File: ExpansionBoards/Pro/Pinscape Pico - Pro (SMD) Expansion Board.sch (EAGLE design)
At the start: 209 parts, among them IC1 UCC27523D, IC10 UCC27523D, IC11 UCC27523D, IC12 UCC27523D, IC13 UCC27523D, IC14 UCC27523D, IC15 TLC59116FIRHBR, IC16 TLC59116FIRHBR, IC17 TLC59116FIRHBR, IC18 TLC59116FIRHBR, IC19 ULN2803ADWR, IC2 UCC27523D, IC20 ULN2803ADWR, IC21 ULN2803ADWR, IC22 ULN2803ADWR, IC23 ULN2803ADWR, IC24 SN74HC165PWR, IC25 SN74HC165PWR, IC26 SN74HC165PWR, IC27 SN74HC165PWR, IC28 LIS3DHTR, IC29 SN74LVC1G175DCKR, IC3 UCC27523D, IC30 APX809S-29SA-7, IC31 LTV-827S, IC32 ADS1115IDGSR, IC33 TLV75733PDBVR, IC34 RV-3032-C7, IC4 UCC27523D, IC5 UCC27523D, IC6 UCC27523D, IC7 UCC27523D, IC8 UCC27523D, IC9 UCC27523D, J1 640445-6, J10 1-640456-0, J11 1-640456-0, J12 1-640456-0, J13 640445-5, J14 640445-9, J15 640445-9, J16 640445-9, J2 30316-6002HB, J3 1-640456-0, J4 640456-9, J5 640456-9, J6 640454-2, J7 215079-4, J8 30308-6002HB, J9 1-640456-0, Q1 BUK7K89-100EX, Q10 BUK7K89-100EX, Q11 BUK7K89-100EX, Q12 BUK7K89-100EX, Q13 BUK7K89-100EX, Q14 BUK7K89-100EX, Q15 UMA5NTR, Q16 UMA5NTR, Q17 UMA5NTR, Q18 UMA5NTR, Q19 UMA5NTR, Q2 BUK7K89-100EX, Q20 UMA5NTR, Q21 UMA5NTR, Q22 UMA5NTR, Q23 UMA5NTR, Q24 UMA5NTR, Q25 UMA5NTR, Q26 UMA5NTR, Q27 DSS8110Y-7, Q3 BUK7K89-100EX, Q4 BUK7K89-100EX, Q5 BUK7K89-100EX, Q6 BUK7K89-100EX, Q7 BUK7K89-100EX, Q8 BUK7K89-100EX, Q9 BUK7K89-100EX, SW1 TS-1187A-B-A-B, U1 BAT-HLD-001-THM

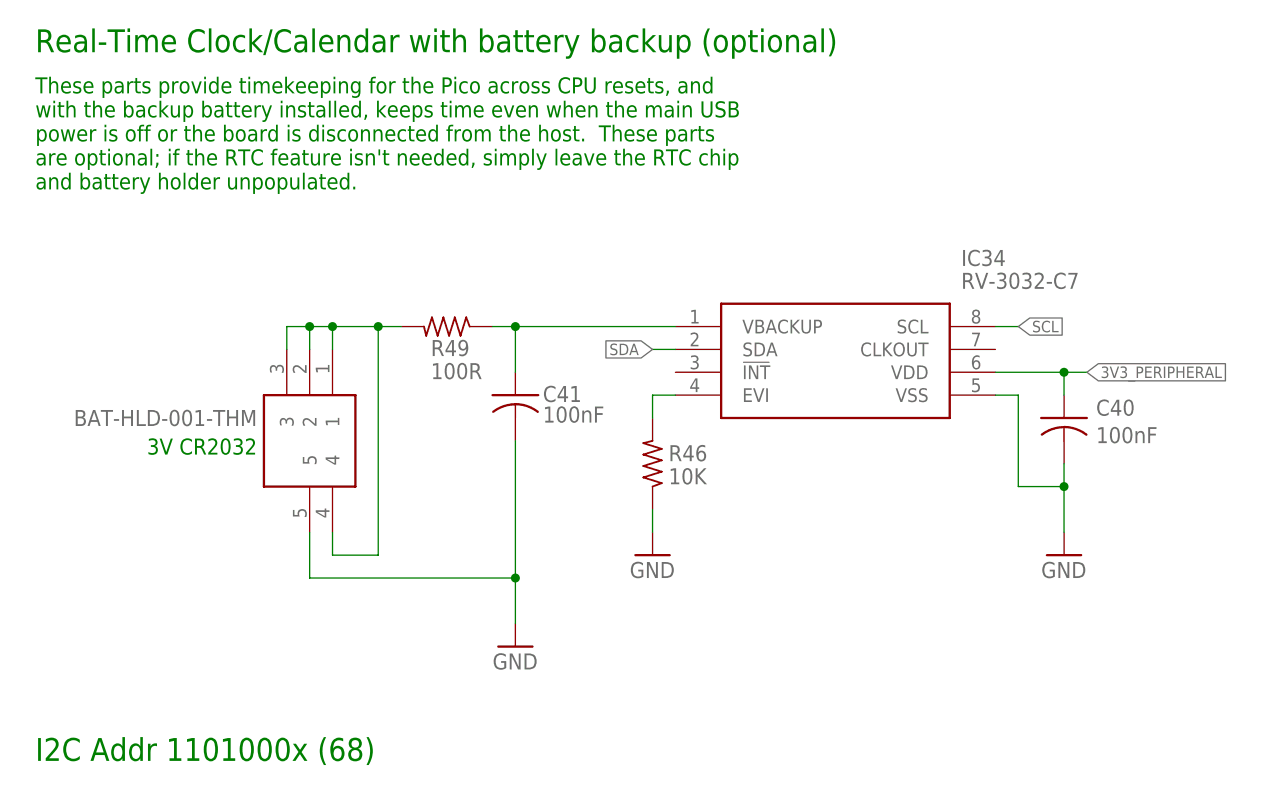
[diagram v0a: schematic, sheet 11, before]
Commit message: exp board: pro: change battery holder to top clip type
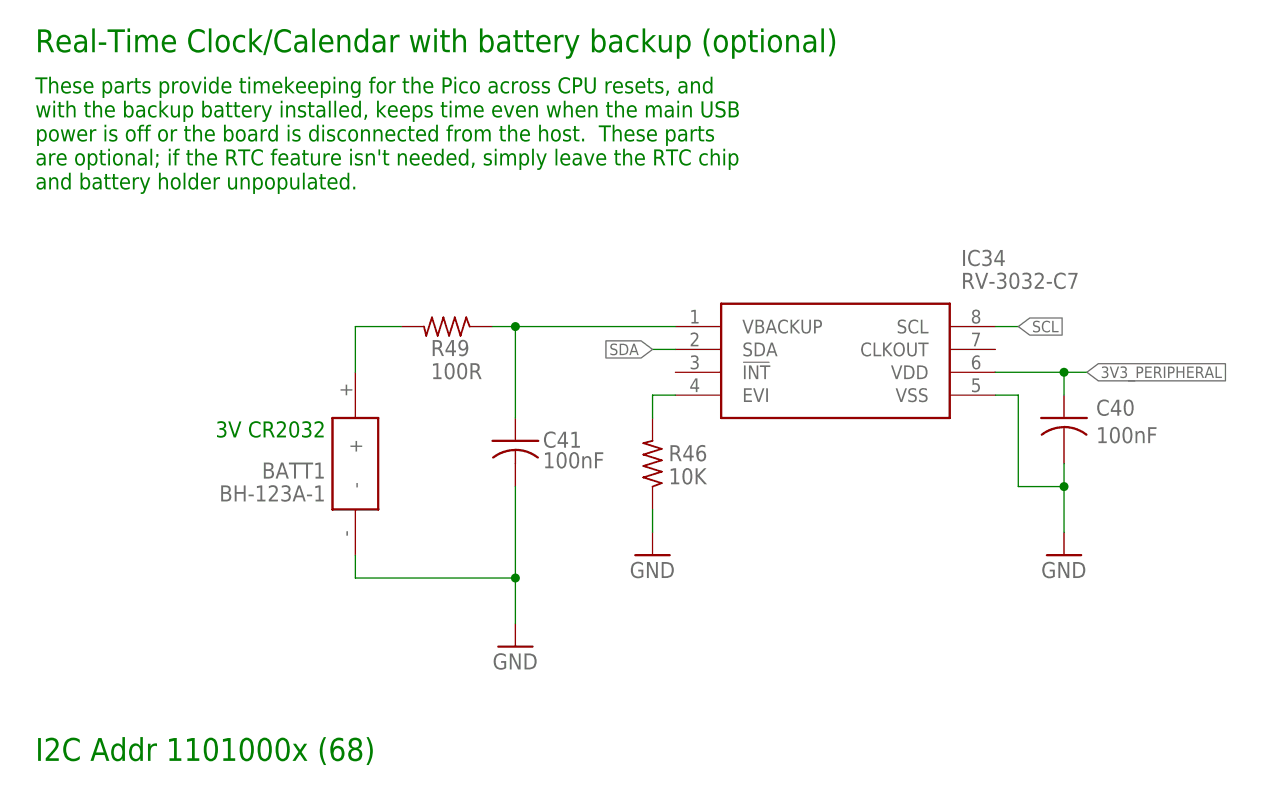
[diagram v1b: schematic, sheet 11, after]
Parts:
- removed U1: BAT-HLD-001-THM, SamacSys_Parts:BAT-HLD-001-THM
- added BATT1: BH-123A-1, SamacSys_Parts:BH-123A-1
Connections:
- net GND: now also BATT1.-; no longer U1.5
- net N$72: now also BATT1.+; no longer U1.1, U1.2, U1.3, U1.4
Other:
- moved on the sheet: C41
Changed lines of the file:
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@@
 <part name="R45" library="resistor" deviceset="R-US_" device="R0603" value="10K"/>
 <part name="C40" library="rcl" deviceset="C-US" device="C0402" value="100nF"/>
-<part name="U1" library="SamacSys_Parts" deviceset="BAT-HLD-001-THM" device=""/>
 <part name="GND30" library="supply1" deviceset="GND" device=""/>
 <part name="GND53" library="supply1" deviceset="GND" device=""/>
@@
 <part name="GND11" library="supply1" deviceset="GND" device=""/>
 <part name="GND12" library="supply1" deviceset="GND" device=""/>
+<part name="BATT1" library="SamacSys_Parts" deviceset="BH-123A-1" device=""/>
 </parts>
 <sheets>
@@
 <description>RTC (Real-time clock)</description>
 <plain>
-<text x="29.718" y="53.594" size="1.778" layer="91" rot="R180">3V CR2032</text>
+<text x="37.338" y="54.61" size="1.778" layer="91" align="center-right">3V CR2032</text>
 <text x="5.08" y="17.78" size="2.54" layer="91">I2C Addr 1101000x (68)</text>
 <text x="5.08" y="96.52" size="2.54" layer="91">Real-Time Clock/Calendar with battery backup (optional)</text>
@@
 <attribute name="VALUE" x="122.936" y="53.086" size="1.778" layer="96"/>
 </instance>
-<instance part="U1" gate="G$1" x="38.1" y="63.5" smashed="yes" rot="R270">
-<attribute name="VALUE" x="29.718" y="55.88" size="1.778" layer="96" rot="R180" align="center-left"/>
-</instance>
 <instance part="GND30" gate="1" x="58.42" y="30.48"/>
 <instance part="GND53" gate="1" x="119.38" y="40.64"/>
-<instance part="C41" gate="G$1" x="58.42" y="58.42" smashed="yes">
-<attribute name="NAME" x="61.468" y="57.658" size="1.778" layer="95"/>
-<attribute name="VALUE" x="61.468" y="55.372" size="1.778" layer="96"/>
+<instance part="C41" gate="G$1" x="58.42" y="53.34" smashed="yes">
+<attribute name="NAME" x="61.468" y="52.578" size="1.778" layer="95"/>
+<attribute name="VALUE" x="61.468" y="50.292" size="1.778" layer="96"/>
 </instance>
 <instance part="IC34" gate="G$1" x="76.2" y="66.04"/>
@@
 <attribute name="VALUE" x="49.022" y="61.976" size="1.778" layer="96" rot="MR180"/>
 </instance>
+<instance part="BATT1" gate="G$1" x="40.64" y="50.8" smashed="yes" rot="R270">
+<attribute name="NAME" x="37.338" y="50.038" size="1.778" layer="95" rot="R180" align="center-left"/>
+<attribute name="VALUE" x="37.338" y="47.498" size="1.778" layer="96" rot="R180" align="center-left"/>
+</instance>
 </instances>
 <busses>
@@
 <net name="GND" class="0">
 <segment>
-<pinref part="U1" gate="G$1" pin="5"/>
 <pinref part="GND30" gate="1" pin="GND"/>
-<wire x1="35.56" y1="43.18" x2="35.56" y2="38.1" width="0.1524" layer="91"/>
 <pinref part="C41" gate="G$1" pin="2"/>
-<wire x1="58.42" y1="53.34" x2="58.42" y2="38.1" width="0.1524" layer="91"/>
-<wire x1="58.42" y1="38.1" x2="35.56" y2="38.1" width="0.1524" layer="91"/>
+<wire x1="58.42" y1="48.26" x2="58.42" y2="38.1" width="0.1524" layer="91"/>
+<pinref part="BATT1" gate="G$1" pin="-"/>
+<wire x1="58.42" y1="38.1" x2="58.42" y2="33.02" width="0.1524" layer="91"/>
+<wire x1="40.64" y1="40.64" x2="40.64" y2="38.1" width="0.1524" layer="91"/>
+<wire x1="40.64" y1="38.1" x2="58.42" y2="38.1" width="0.1524" layer="91"/>
 <junction x="58.42" y="38.1"/>
-<wire x1="58.42" y1="33.02" x2="58.42" y2="38.1" width="0.1524" layer="91"/>
 </segment>
 <segment>
@@
 </segment>
 </net>
-<net name="N$72" class="0">
-<segment>
-<pinref part="U1" gate="G$1" pin="4"/>
-<wire x1="38.1" y1="43.18" x2="38.1" y2="40.64" width="0.1524" layer="91"/>
-<wire x1="38.1" y1="40.64" x2="43.18" y2="40.64" width="0.1524" layer="91"/>
-<wire x1="43.18" y1="40.64" x2="43.18" y2="66.04" width="0.1524" layer="91"/>
-<pinref part="U1" gate="G$1" pin="1"/>
-<wire x1="38.1" y1="63.5" x2="38.1" y2="66.04" width="0.1524" layer="91"/>
-<pinref part="U1" gate="G$1" pin="2"/>
-<wire x1="35.56" y1="63.5" x2="35.56" y2="66.04" width="0.1524" layer="91"/>
-<wire x1="38.1" y1="66.04" x2="35.56" y2="66.04" width="0.1524" layer="91"/>
-<pinref part="U1" gate="G$1" pin="3"/>
-<wire x1="33.02" y1="63.5" x2="33.02" y2="66.04" width="0.1524" layer="91"/>
-<junction x="35.56" y="66.04"/>
-<wire x1="43.18" y1="66.04" x2="38.1" y2="66.04" width="0.1524" layer="91"/>
-<junction x="38.1" y="66.04"/>
-<wire x1="35.56" y1="66.04" x2="33.02" y2="66.04" width="0.1524" layer="91"/>
-<pinref part="R49" gate="G$1" pin="2"/>
-<wire x1="43.18" y1="66.04" x2="45.72" y2="66.04" width="0.1524" layer="91"/>
-<junction x="43.18" y="66.04"/>
-</segment>
-</net>
 <net name="3V3_PERIPHERAL" class="0">
 <segment>
@@
 <wire x1="58.42" y1="66.04" x2="76.2" y2="66.04" width="0.1524" layer="91"/>
 <pinref part="C41" gate="G$1" pin="1"/>
-<wire x1="58.42" y1="60.96" x2="58.42" y2="66.04" width="0.1524" layer="91"/>
+<wire x1="58.42" y1="55.88" x2="58.42" y2="66.04" width="0.1524" layer="91"/>
 <pinref part="R49" gate="G$1" pin="1"/>
 <wire x1="55.88" y1="66.04" x2="58.42" y2="66.04" width="0.1524" layer="91"/>
@@
 </segment>
 </net>
+<net name="N$72" class="0">
+<segment>
+<pinref part="R49" gate="G$1" pin="2"/>
+<wire x1="45.72" y1="66.04" x2="40.64" y2="66.04" width="0.1524" layer="91"/>
+<pinref part="BATT1" gate="G$1" pin="+"/>
+<wire x1="40.64" y1="66.04" x2="40.64" y2="60.96" width="0.1524" layer="91"/>
+</segment>
+</net>

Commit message: exp board: Pro: change ULN2803ADWR to -CDWR (-ADWR is EOL, replacement is -CDWR)
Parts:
- IC19, IC20, IC21, IC22, IC23: value ULN2803ADWR -> ULN2803CDWR; device SamacSys_Parts:ULN2803ADWR -> SamacSys_Parts:ULN2803CDWR

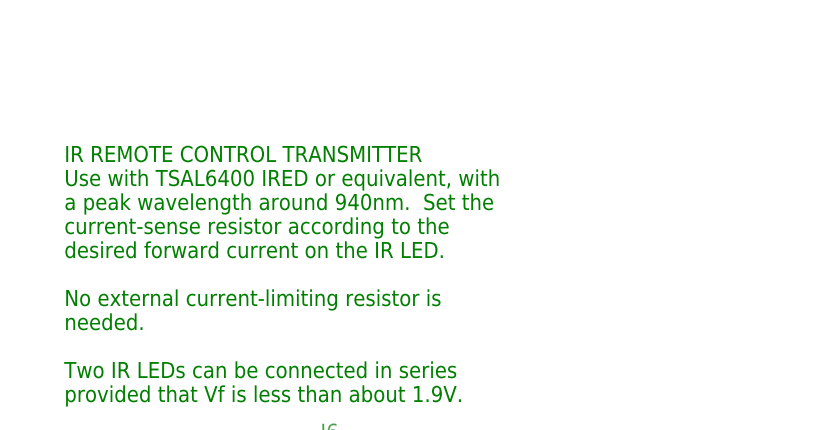
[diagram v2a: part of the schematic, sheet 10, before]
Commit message: Improve expansion board IR receiver documentation
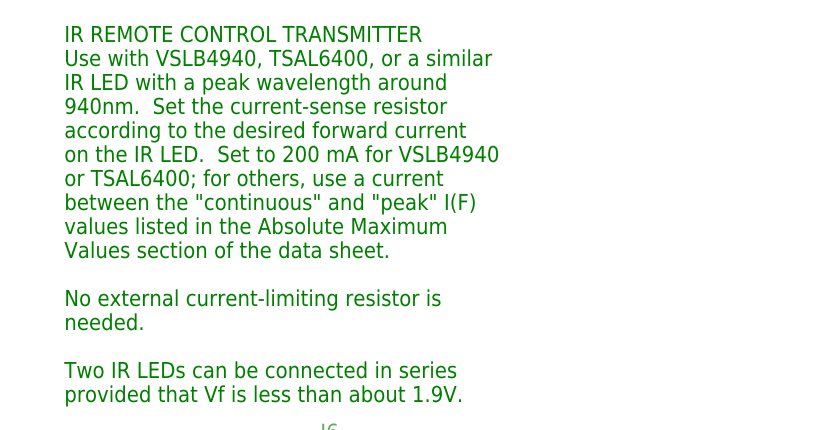
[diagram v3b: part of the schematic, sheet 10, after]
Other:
- note added: "IR REMOTE CONTROL TRANSMITTER Use with VSLB4940, TSAL6400, or a similar IR LED with a peak wavelength around 940nm. Set the current-sense resistor according to the desired forward current on the IR LED. Set to 200 mA for VSLB4940 or TSAL6400; for others, use a current between the "continuous" and "peak" I(F) values listed in the Absolute Maximum Values section of the data sheet. No external curre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"
- note removed: "IR REMOTE CONTROL TRANSMITTER Use with TSAL6400 IRED or equivalent, with a peak wavelength around 940nm. Set the current-sense resistor according to the desired forward current on the IR LED. No external current-limiting resistor is needed. Two IR LEDs can be connected in series provided that Vf is less than about 1.9V."
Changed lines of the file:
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@@
 R=2.5 ohms -&gt; 200mA current</text>
 <text x="7.62" y="81.28" size="1.778" layer="91">IR REMOTE CONTROL TRANSMITTER
-Use with TSAL6400 IRED or equivalent, with
-a peak wavelength around 940nm.  Set the
-current-sense resistor according to the
-desired forward current on the IR LED.
+Use with VSLB4940, TSAL6400, or a similar
+IR LED with a peak wavelength around
+940nm.  Set the current-sense resistor
+according to the desired forward current
+on the IR LED.  Set to 200 mA for VSLB4940
+or TSAL6400; for others, use a current
+between the "continuous" and "peak" I(F)
+values listed in the Absolute Maximum
+Values section of the data sheet.
 No external current-limiting resistor is
 needed.
